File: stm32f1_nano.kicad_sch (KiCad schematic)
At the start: 50 parts, among them J1 Analog, J2 Digital, J3 TYPE-C-31-M-12, J4 Conn_ST_STDC14, J5 DEBUG, Q1 AO3401A, U1 STM32F103C8T6, U2 W25Q128JVSIQ, U3 AMS1117-3.3, U4 XC6206P332MR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

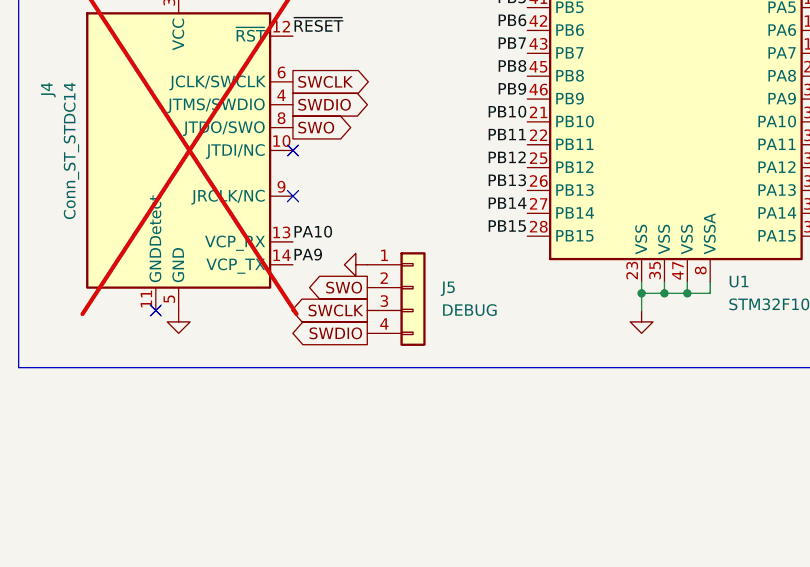
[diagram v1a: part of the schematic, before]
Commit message: #1 Make debug pins compatible with BluePill
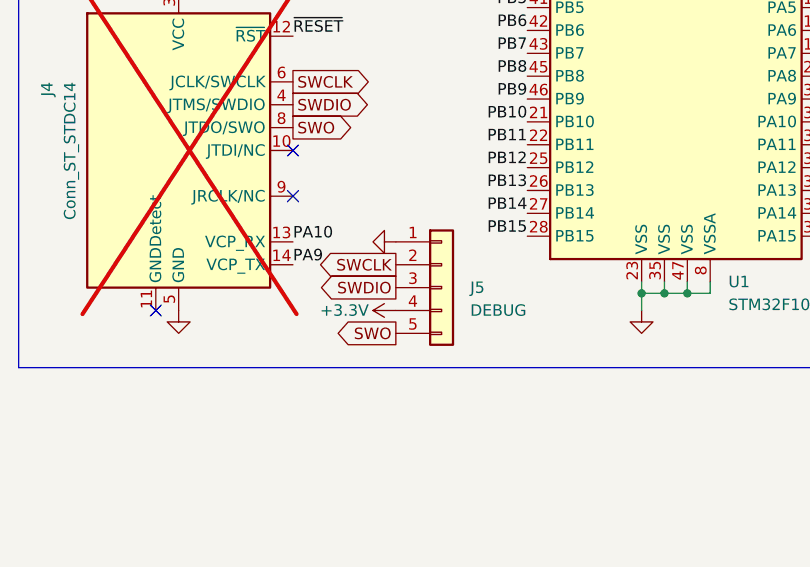
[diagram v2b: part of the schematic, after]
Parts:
- J5: footprint Connector_PinHeader_2.54mm:PinHeader_1x04_P2.54mm_Vertical -> Connector_PinHeader_2.54mm:PinHeader_1x05_P2.54mm_Vertical; symbol Connector_Generic:Conn_01x04 -> Connector_Generic:Conn_01x05; now in the parts list
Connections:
- net +3.3V: now also J5.4 (Pin_4)
- net SWCLK: now also J5.2 (Pin_2); no longer J5.3 (Pin_3)
- net SWDIO: now also J5.3 (Pin_3); no longer J5.4 (Pin_4)
- net SWO: now also J5.5 (Pin_5); no longer J5.2 (Pin_2)
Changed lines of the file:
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@@
     (effects (font (size 1.27 1.27)) (justify left bottom))
   )
-  (global_label "SWO" (shape output) (at 128.905 118.11 180) (fields_autoplaced)
+  (global_label "SWO" (shape output) (at 132.08 123.19 180) (fields_autoplaced)
     (effects (font (size 1.27 1.27)) (justify right))
-    (property "Intersheetrefs" "${INTERSHEET_REFS}" (at 121.8333 118.11 0)
+    (property "Intersheetrefs" "${INTERSHEET_REFS}" (at 125.0083 123.19 0)
       (effects (font (size 1.27 1.27)) (justify right) hide)
     )
   )
-  (global_label "SWDIO" (shape output) (at 128.905 123.19 180) (fields_autoplaced)
+  (global_label "SWDIO" (shape output) (at 132.08 118.11 180) (fields_autoplaced)
     (effects (font (size 1.27 1.27)) (justify right))
-    (property "Intersheetrefs" "${INTERSHEET_REFS}" (at 119.9585 123.19 0)
+    (property "Intersheetrefs" "${INTERSHEET_REFS}" (at 123.1335 118.11 0)
       (effects (font (size 1.27 1.27)) (justify right) hide)
     )
@@
     )
   )
-  (global_label "SWCLK" (shape output) (at 128.905 120.65 180) (fields_autoplaced)
+  (global_label "SWCLK" (shape output) (at 132.08 115.57 180) (fields_autoplaced)
     (effects (font (size 1.27 1.27)) (justify right))
-    (property "Intersheetrefs" "${INTERSHEET_REFS}" (at 119.5957 120.65 0)
+    (property "Intersheetrefs" "${INTERSHEET_REFS}" (at 122.7707 115.57 0)
       (effects (font (size 1.27 1.27)) (justify right) hide)
     )
@@
     )
   )
-  (symbol (lib_id "Connector_Generic:Conn_01x04") (at 133.985 118.11 0) (unit 1)
-    (in_bom no) (on_board yes) (dnp no) (fields_autoplaced)
-    (property "Reference" "J5" (at 137.16 118.11 0)
+  (symbol (lib_id "Connector_Generic:Conn_01x05") (at 137.16 118.11 0) (unit 1)
+    (in_bom yes) (on_board yes) (dnp no) (fields_autoplaced)
+    (property "Reference" "J5" (at 140.335 118.11 0)
       (effects (font (size 1.27 1.27)) (justify left))
     )
-    (property "Value" "DEBUG" (at 137.16 120.65 0)
+    (property "Value" "DEBUG" (at 140.335 120.65 0)
       (effects (font (size 1.27 1.27)) (justify left))
     )
-    (property "Footprint" "Connector_PinHeader_2.54mm:PinHeader_1x04_P2.54mm_Vertical" (at 133.985 118.11 0)
-      (effects (font (size 1.27 1.27)) hide)
-    )
-    (property "Datasheet" "~" (at 133.985 118.11 0)
-      (effects (font (size 1.27 1.27)) hide)
-    )
-    (property "Description" "" (at 133.985 118.11 0)
-      (effects (font (size 1.27 1.27)) hide)
-    )
-    (property "Manufacturer" "" (at 133.985 118.11 0)
-      (effects (font (size 1.27 1.27)) hide)
-    )
-    (property "Partnumber" "" (at 133.985 118.11 0)
-      (effects (font (size 1.27 1.27)) hide)
-    )
-    (property "JLCPCB Part #" "" (at 133.985 118.11 0)
-      (effects (font (size 1.27 1.27)) hide)
-    )
-    (property "isBasicPart" "" (at 133.985 118.11 0)
-      (effects (font (size 1.27 1.27)) hide)
-    )
-    (property "Description" "" (at 133.985 118.11 0)
-      (effects (font (size 1.27 1.27)) hide)
-    )
-    (property "Manufacturer" "" (at 133.985 118.11 0)
-      (effects (font (size 1.27 1.27)) hide)
-    )
-    (property "Partnumber" "" (at 133.985 118.11 0)
-      (effects (font (size 1.27 1.27)) hide)
-    )
-    (property "JLCPCB Part #" "" (at 133.985 118.11 0)
-      (effects (font (size 1.27 1.27)) hide)
-    )
-    (property "isBasicPart" "" (at 133.985 118.11 0)
+    (property "Footprint" "Connector_PinHeader_2.54mm:PinHeader_1x05_P2.54mm_Vertical" (at 137.16 118.11 0)
+      (effects (font (size 1.27 1.27)) hide)
+    )
+    (property "Datasheet" "~" (at 137.16 118.11 0)
+      (effects (font (size 1.27 1.27)) hide)
+    )
+    (property "Description" "" (at 137.16 118.11 0)
+      (effects (font (size 1.27 1.27)) hide)
+    )
+    (property "Manufacturer" "" (at 137.16 118.11 0)
+      (effects (font (size 1.27 1.27)) hide)
+    )
+    (property "Partnumber" "" (at 137.16 118.11 0)
+      (effects (font (size 1.27 1.27)) hide)
+    )
+    (property "JLCPCB Part #" "" (at 137.16 118.11 0)
+      (effects (font (size 1.27 1.27)) hide)
+    )
+    (property "isBasicPart" "" (at 137.16 118.11 0)
+      (effects (font (size 1.27 1.27)) hide)
+    )
+    (property "Description" "" (at 137.16 118.11 0)
+      (effects (font (size 1.27 1.27)) hide)
+    )
+    (property "Manufacturer" "" (at 137.16 118.11 0)
+      (effects (font (size 1.27 1.27)) hide)
+    )
+    (property "Partnumber" "" (at 137.16 118.11 0)
+      (effects (font (size 1.27 1.27)) hide)
+    )
+    (property "JLCPCB Part #" "" (at 137.16 118.11 0)
+      (effects (font (size 1.27 1.27)) hide)
+    )
+    (property "isBasicPart" "" (at 137.16 118.11 0)
       (effects (font (size 1.27 1.27)) hide)
     )
@@
     (pin "3")
     (pin "4")
+    (pin "5")
     (instances
       (project "stm32f1_nano"
@@
     )
   )
-  (symbol (lib_id "power:GND") (at 128.905 115.57 270) (unit 1)
+  (symbol (lib_id "power:GND") (at 132.08 113.03 270) (unit 1)
     (in_bom yes) (on_board yes) (dnp no) (fields_autoplaced)
-    (property "Reference" "#PWR0101" (at 122.555 115.57 0)
-      (effects (font (size 1.27 1.27)) hide)
-    )
-    (property "Value" "GND" (at 123.825 115.57 0)
-      (effects (font (size 1.27 1.27)) hide)
-    )
-    (property "Footprint" "" (at 128.905 115.57 0)
-      (effects (font (size 1.27 1.27)) hide)
-    )
-    (property "Datasheet" "" (at 128.905 115.57 0)
+    (property "Reference" "#PWR0101" (at 125.73 113.03 0)
+      (effects (font (size 1.27 1.27)) hide)
+    )
+    (property "Value" "GND" (at 127 113.03 0)
+      (effects (font (size 1.27 1.27)) hide)
+    )
+    (property "Footprint" "" (at 132.08 113.03 0)
+      (effects (font (size 1.27 1.27)) hide)
+    )
+    (property "Datasheet" "" (at 132.08 113.03 0)
       (effects (font (size 1.27 1.27)) hide)
     )
@@
         )
       )
+    )
+  )
+  (symbol (lib_id "power:+3.3V") (at 132.08 120.65 90) (unit 1)
+    (in_bom yes) (on_board yes) (dnp no)
+    (property "Reference" "#PWR018" (at 135.89 120.65 0)
+      (effects (font (size 1.27 1.27)) hide)
+    )
+    (property "Value" "+3.3V" (at 126.365 120.65 90)
+      (effects (font (size 1.27 1.27)))
+    )
+    (property "Footprint" "" (at 132.08 120.65 0)
+      (effects (font (size 1.27 1.27)) hide)
+    )
+    (property "Datasheet" "" (at 132.08 120.65 0)
+      (effects (font (size 1.27 1.27)) hide)
+    )
+    (pin "1")
+    (instances
+      (project "stm32f1_nano"
+        (path "/0d35483a-0b12-46cc-b9f2-896fd6831779"
+          (reference "#PWR018") (unit 1)
+        )
+      )
+      (project "stm32f1"
+        (path "/5e832605-8ffe-4662-837d-abaa536d3f2c"
+          (reference "#PWR0104") (unit 1)
+        )
+      )

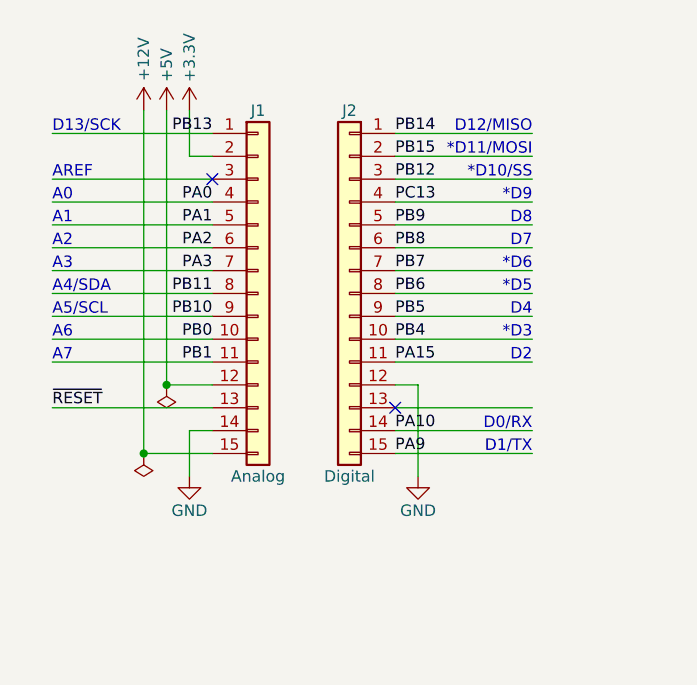
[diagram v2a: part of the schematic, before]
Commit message: #5 Check PWM pins
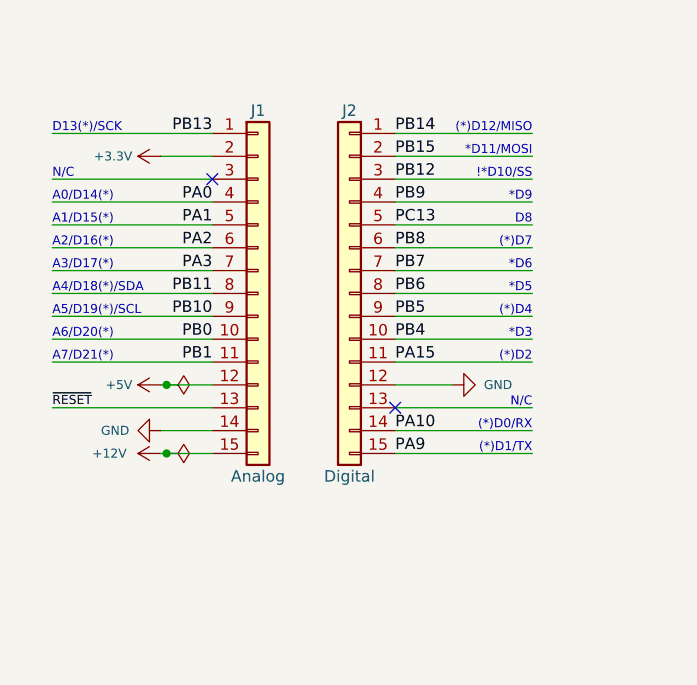
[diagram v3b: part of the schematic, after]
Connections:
- net PB9: now also J2.4 (Pin_4); no longer J2.5 (Pin_5)
- net PC13: now also J2.5 (Pin_5); no longer J2.4 (Pin_4)
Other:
- note added: "!*D10/SS"
- note added: "(*)D0/RX"
- note added: "(*)D1/TX"
- note added: "(*)D12/MISO"
- note added: "(*)D2"
- note added: "(*)D4"
- note added: "(*)D7"
- note added: "A0/D14(*)"
- note added: "A1/D15(*)"
- note added: "A2/D16(*)"
- note added: "A3/D17(*)"
- note added: "A4/D18(*)/SDA"
- note added: "A5/D19(*)/SCL"
- note added: "A6/D20(*)"
- note added: "A7/D21(*)"
- note added: "D13(*)/SCK"
- note added: "N/C"
- note removed: "*D10/SS"
- note removed: "A0"
- note removed: "A1"
- note removed: "A2"
- note removed: "A3"
- note removed: "A4/SDA"
- note removed: "A5/SCL"
- note removed: "A6"
- note removed: "A7"
- note removed: "AREF"
- note removed: "D0/RX"
- note removed: "D1/TX"
- note removed: "D12/MISO"
- note removed: "D13/SCK"
- note removed: "D2"
- note removed: "D4"
- note removed: "D7"
